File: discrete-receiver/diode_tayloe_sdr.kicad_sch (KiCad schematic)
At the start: 7 parts, among them J2 Optional 5V DC Jack, J3 USB_C_Receptacle_USB2.0_16P, X1 YC24.576MUBCE2O

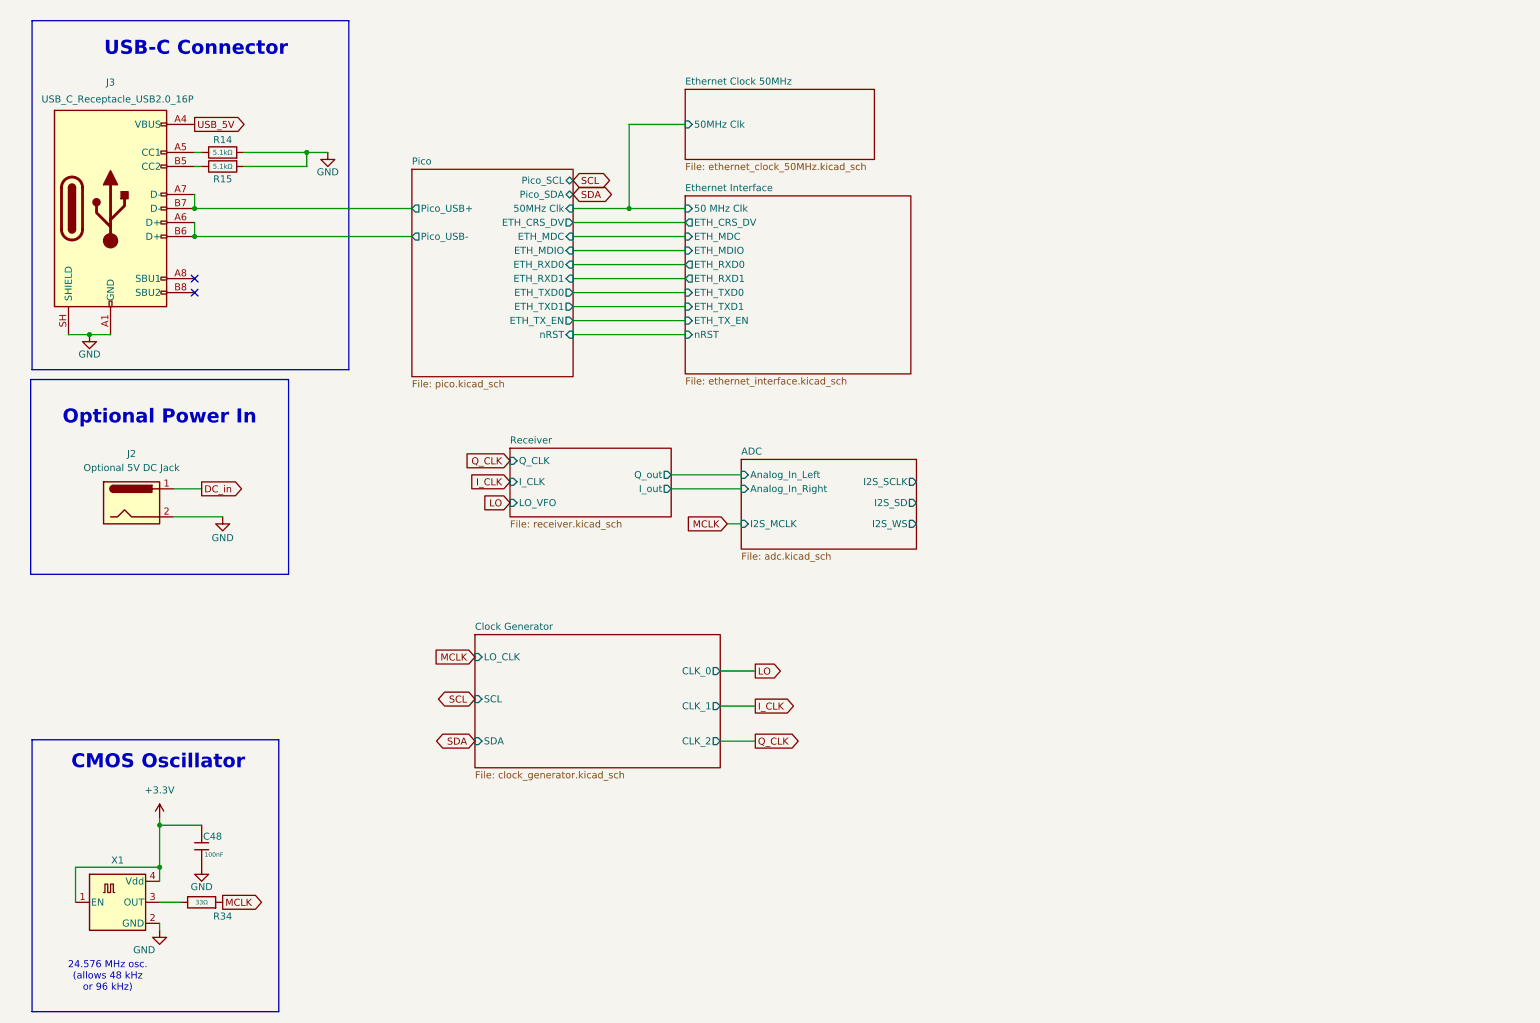
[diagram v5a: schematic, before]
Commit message: Organized Schematic
Standardized component labelling and font sizes. Added descriptions to some sub sheets and organized layout of root sheet.
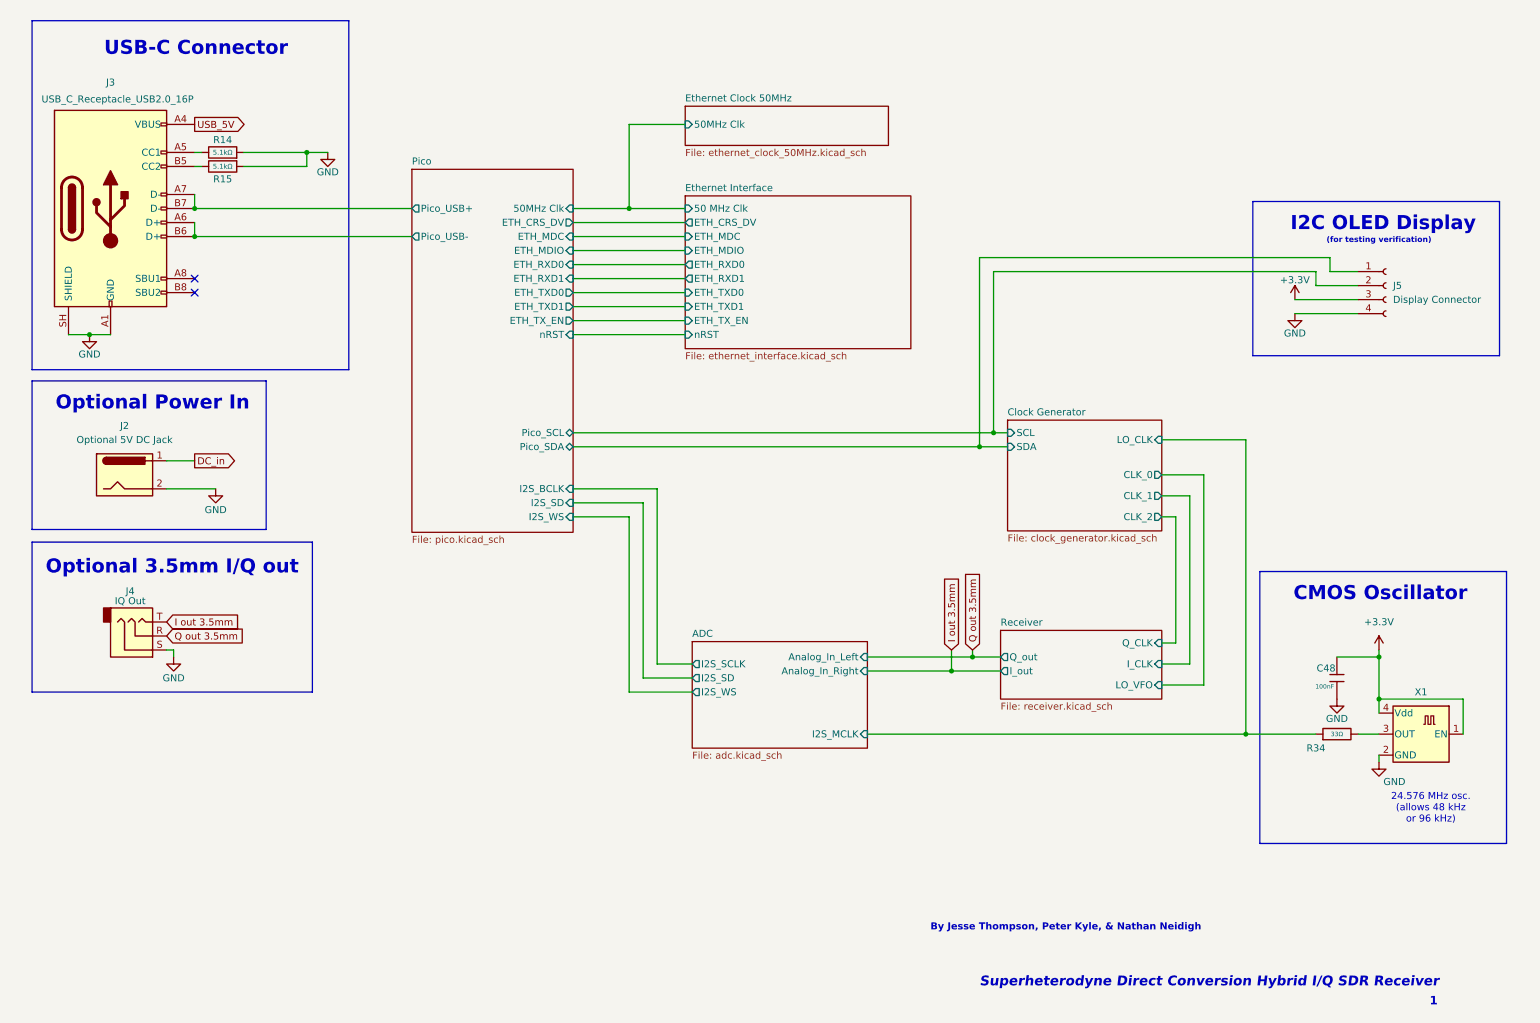
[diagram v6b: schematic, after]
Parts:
- added J4: IQ Out, symbol Connector_Audio:AudioJack3
- added J5: Display Connector, symbol Connector:Conn_01x04_Socket
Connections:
- net +3.3V: now also J5.3 (Pin_3)
- net GND: now also J4.S, J5.4 (Pin_4)
- net MCLK renamed ADC/I2S_MCLK
- new net Clock Generator/SCL: J5.2 (Pin_2)
- new net Clock Generator/SDA: J5.1 (Pin_1)
- new net I out 3.5mm: J4.T
- new net Q out 3.5mm: J4.R
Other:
- sheet Pico ports: added I2S_BCLK, I2S_SD, I2S_WS; removed none
- note added: "(for testing verification)"
- note added: "1"
- note added: "By Jesse Thompson, Peter Kyle, & Nathan Neidigh"
- note added: "I2C OLED Display"
- note added: "Optional 3.5mm I/Q out"
- note added: "Superheterodyne Direct Conversion Hybrid I/Q SDR Receiver"
- moved on the sheet: C48, J2, R34, X1

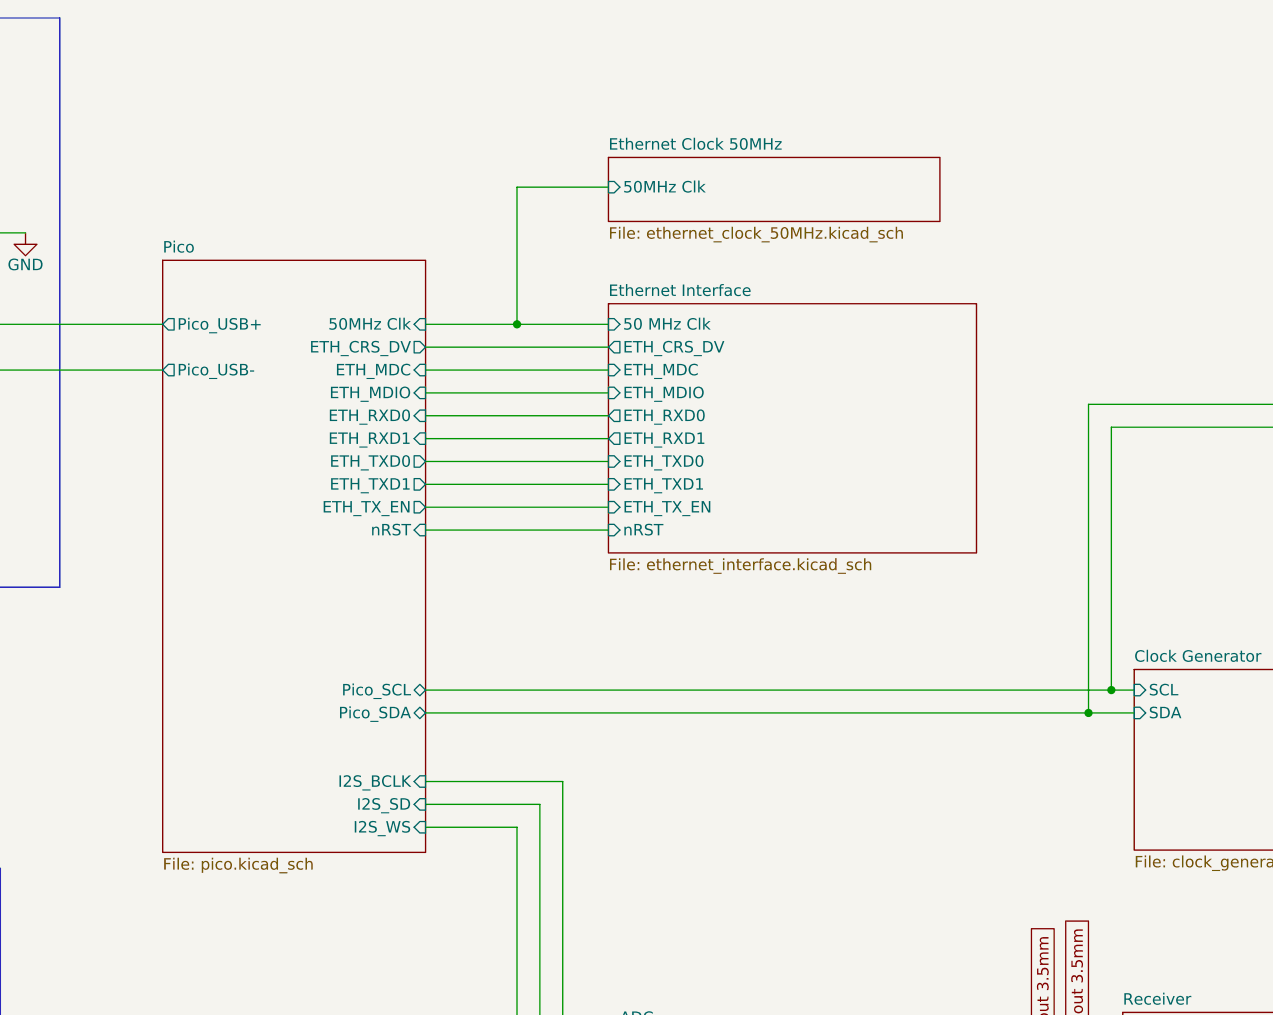
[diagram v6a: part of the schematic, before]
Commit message: Updated ethernet clocking details
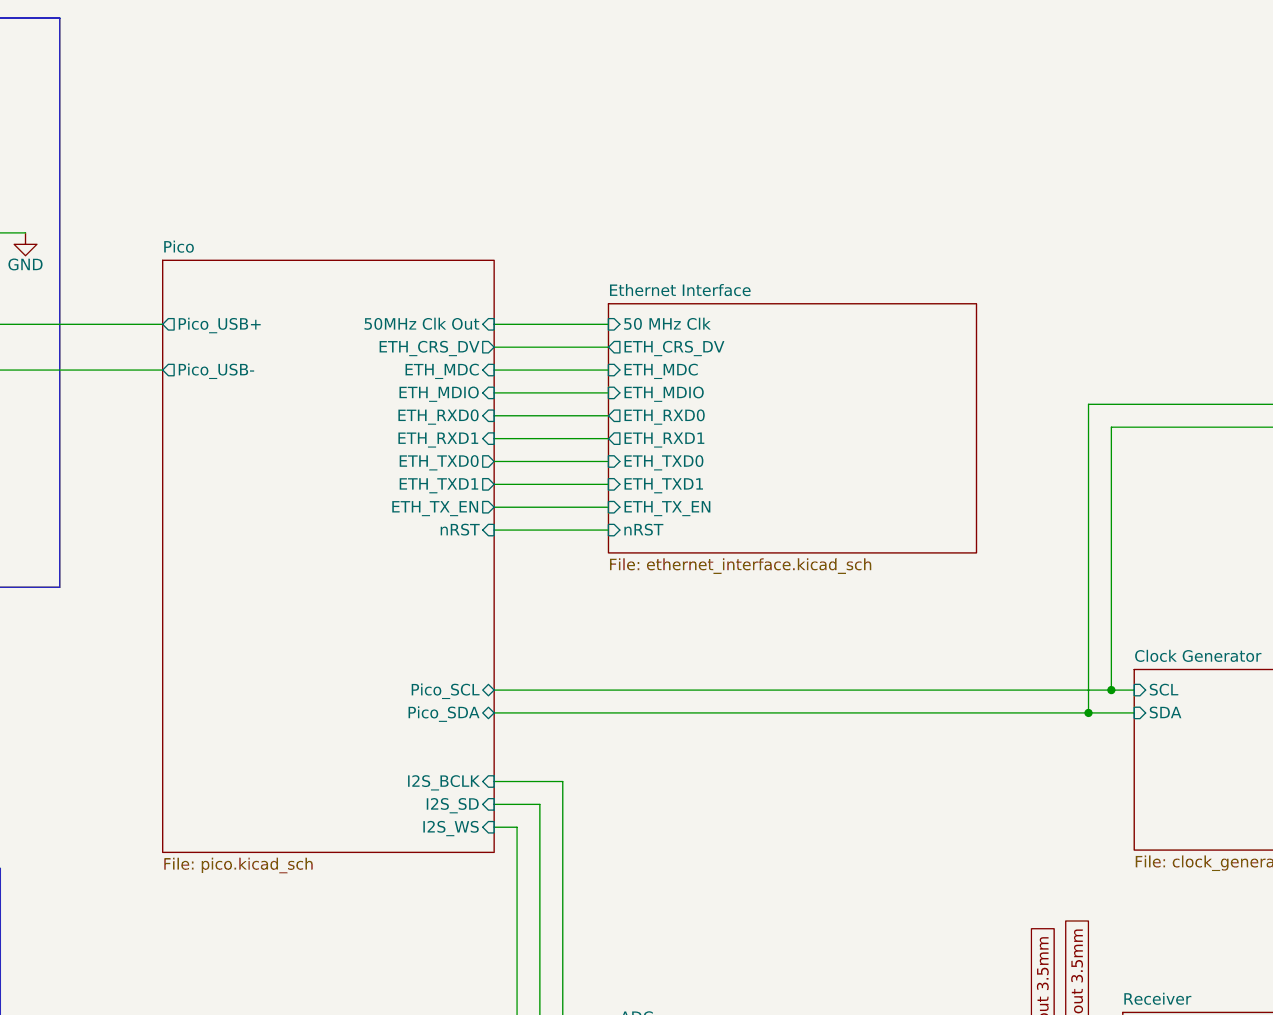
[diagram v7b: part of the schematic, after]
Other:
- removed sheet Ethernet Clock 50MHz
- sheet Pico ports: added 50MHz Clk Out; removed 50MHz Clk
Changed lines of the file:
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@@
 		(color 0 0 0 0)
 	)
-	(junction
-		(at 123.19 49.53)
-		(diameter 0)
-		(color 0 0 0 0)
-	)
 	(no_connect
 		(at 44.45 62.23)
@@
 	(wire
 		(pts
-			(xy 123.19 34.29) (xy 123.19 49.53)
-		)
-		(stroke
-			(width 0)
-			(type default)
-		)
-	)
-	(wire
-		(pts
 			(xy 44.45 52.07) (xy 44.45 54.61)
 		)
@@
 	(wire
 		(pts
-			(xy 113.03 62.23) (xy 133.35 62.23)
+			(xy 120.65 62.23) (xy 133.35 62.23)
 		)
 		(stroke
@@
 	(wire
 		(pts
-			(xy 113.03 54.61) (xy 133.35 54.61)
+			(xy 120.65 54.61) (xy 133.35 54.61)
 		)
 		(stroke
@@
 	(wire
 		(pts
-			(xy 113.03 105.41) (xy 123.19 105.41)
+			(xy 120.65 105.41) (xy 123.19 105.41)
 		)
 		(stroke
@@
 	(wire
 		(pts
-			(xy 133.35 34.29) (xy 123.19 34.29)
-		)
-		(stroke
-			(width 0)
-			(type default)
-		)
-	)
-	(wire
-		(pts
 			(xy 64.77 41.91) (xy 64.77 39.37)
 		)
@@
 	(wire
 		(pts
-			(xy 113.03 57.15) (xy 133.35 57.15)
+			(xy 120.65 57.15) (xy 133.35 57.15)
 		)
 		(stroke
@@
 	(wire
 		(pts
-			(xy 113.03 100.33) (xy 128.27 100.33)
+			(xy 120.65 100.33) (xy 128.27 100.33)
 		)
 		(stroke
@@
 	(wire
 		(pts
-			(xy 123.19 49.53) (xy 133.35 49.53)
+			(xy 120.65 49.53) (xy 133.35 49.53)
 		)
 		(stroke
@@
 	(wire
 		(pts
-			(xy 113.03 72.39) (xy 133.35 72.39)
+			(xy 120.65 72.39) (xy 133.35 72.39)
 		)
 		(stroke
@@
 	(wire
 		(pts
-			(xy 113.03 67.31) (xy 133.35 67.31)
+			(xy 120.65 67.31) (xy 133.35 67.31)
 		)
 		(stroke
@@
 	(wire
 		(pts
-			(xy 113.03 90.17) (xy 189.23 90.17)
+			(xy 120.65 90.17) (xy 189.23 90.17)
 		)
 		(stroke
@@
 	(wire
 		(pts
-			(xy 113.03 59.69) (xy 133.35 59.69)
+			(xy 120.65 59.69) (xy 133.35 59.69)
 		)
 		(stroke
@@
 	(wire
 		(pts
-			(xy 113.03 64.77) (xy 133.35 64.77)
+			(xy 120.65 64.77) (xy 133.35 64.77)
 		)
 		(stroke
@@
 	(wire
 		(pts
-			(xy 113.03 92.71) (xy 186.69 92.71)
+			(xy 120.65 92.71) (xy 186.69 92.71)
 		)
 		(stroke
@@
 	(wire
 		(pts
-			(xy 113.03 49.53) (xy 123.19 49.53)
-		)
-		(stroke
-			(width 0)
-			(type default)
-		)
-	)
-	(wire
-		(pts
 			(xy 219.71 97.79) (xy 227.33 97.79)
 		)
@@
 	(wire
 		(pts
-			(xy 113.03 52.07) (xy 133.35 52.07)
+			(xy 120.65 52.07) (xy 133.35 52.07)
 		)
 		(stroke
@@
 	(wire
 		(pts
-			(xy 113.03 69.85) (xy 133.35 69.85)
+			(xy 120.65 69.85) (xy 133.35 69.85)
 		)
 		(stroke
@@
 	(wire
 		(pts
-			(xy 113.03 102.87) (xy 125.73 102.87)
+			(xy 120.65 102.87) (xy 125.73 102.87)
 		)
 		(stroke
@@
 	)
 	(sheet
-		(at 133.35 30.988)
-		(size 36.83 7.112)
-		(exclude_from_sim no)
-		(in_bom yes)
-		(on_board yes)
-		(dnp no)
-		(fields_autoplaced yes)
-		(stroke
-			(width 0.1524)
-			(type solid)
-		)
-		(fill
-			(color 0 0 0 0)
-		)
-		(property "Sheetname" "Ethernet Clock 50MHz"
-			(at 133.35 30.2764 0)
-			(show_name no)
-			(do_not_autoplace no)
-			(effects
-				(font
-					(size 1.27 1.27)
-				)
-				(justify left bottom)
-			)
-		)
-		(property "Sheetfile" "ethernet_clock_50MHz.kicad_sch"
-			(at 133.35 38.6846 0)
-			(show_name no)
-			(do_not_autoplace no)
-			(effects
-				(font
-					(size 1.27 1.27)
-				)
-				(justify left top)
-			)
-		)
-		(pin "50MHz Clk" input
-			(at 133.35 34.29 180)
-			(effects
-				(font
-					(size 1.27 1.27)
-				)
-				(justify left)
-			)
-		)
-		(instances
-			(project "diode_tayloe_sdr"
-				(path "/d18d178d-3f10-4d68-9036-eae71a7d091a"
-					(page "7")
-				)
-			)
-		)
-	)
-	(sheet
 		(at 191.77 87.884)
 		(size 27.94 20.066)
@@
 	(sheet
 		(at 83.82 42.418)
-		(size 29.21 65.786)
+		(size 36.83 65.786)
 		(exclude_from_sim no)
 		(in_bom yes)
@@
 		)
 		(pin "Pico_SCL" bidirectional
-			(at 113.03 90.17 0)
+			(at 120.65 90.17 0)
 			(effects
 				(font
@@
 		)
 		(pin "Pico_SDA" bidirectional
-			(at 113.03 92.71 0)
-			(effects
-				(font
-					(size 1.27 1.27)
-				)
-				(justify right)
-			)
-		)
-		(pin "50MHz Clk" input
-			(at 113.03 49.53 0)
+			(at 120.65 92.71 0)
 			(effects
 				(font
@@
 		)
 		(pin "ETH_CRS_DV" output
-			(at 113.03 52.07 0)
+			(at 120.65 52.07 0)
 			(effects
 				(font
@@
 		)
 		(pin "ETH_MDC" input
-			(at 113.03 54.61 0)
+			(at 120.65 54.61 0)
 			(effects
 				(font
@@
 		)
 		(pin "ETH_MDIO" input
-			(at 113.03 57.15 0)
+			(at 120.65 57.15 0)
 			(effects
 				(font
@@
 		)
 		(pin "ETH_RXD0" input
-			(at 113.03 59.69 0)
+			(at 120.65 59.69 0)
 			(effects
 				(font
@@
 		)
 		(pin "ETH_RXD1" input
-			(at 113.03 62.23 0)
+			(at 120.65 62.23 0)
 			(effects
 				(font
@@
 		)
 		(pin "ETH_TXD0" output
-			(at 113.03 64.77 0)
+			(at 120.65 64.77 0)
 			(effects
 				(font
@@
 		)
 		(pin "ETH_TXD1" output
-			(at 113.03 67.31 0)
+			(at 120.65 67.31 0)
 			(effects
 				(font
@@
 		)
 		(pin "ETH_TX_EN" output
-			(at 113.03 69.85 0)
+			(at 120.65 69.85 0)
 			(effects
 				(font
@@
 		)
 		(pin "nRST" input
-			(at 113.03 72.39 0)
+			(at 120.65 72.39 0)
 			(effects
 				(font
@@
 		)
 		(pin "I2S_BCLK" input
-			(at 113.03 100.33 0)
+			(at 120.65 100.33 0)
 			(effects
 				(font
@@
 		)
 		(pin "I2S_SD" input
-			(at 113.03 102.87 0)
+			(at 120.65 102.87 0)
 			(effects
 				(font
@@
 		)
 		(pin "I2S_WS" input
-			(at 113.03 105.41 0)
+			(at 120.65 105.41 0)
+			(effects
+				(font
+					(size 1.27 1.27)
+				)
+				(justify right)
+			)
+		)
+		(pin "50MHz Clk Out" input
+			(at 120.65 49.53 0)
 			(effects
 				(font

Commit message: Added some notes and stuff
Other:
- note added: "rp2350 generates 50MHz clock from its external 12MHz clock"
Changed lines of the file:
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@@
+		)
+	)
+	(text "rp2350 generates 50MHz clock from its external 12MHz clock"
+		(exclude_from_sim no)
+		(at 154.686 40.894 0)
+		(effects
+			(font
+				(size 1.27 1.27)
+			)
 		)
 	)
